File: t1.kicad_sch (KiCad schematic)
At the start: 47 parts, among them J1 Barrel_Jack_Switch, J2 USB_B, J3 P1, J4 2x2M, J5 ICSP1, J6 P2, U1 ATmega8U2-AU, Y1 16MHz

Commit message: Updated symbols to the ones currently used by KiCad
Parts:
- C1: symbol Device:CP -> Device:C_Polarized
- FB1: symbol Device:Ferrite_Bead -> Device:FerriteBead
- U1: symbol MCU_Microchip_ATmega:ATmega8U2-AU -> MCU_Microchip_ATmega:ATmega8U2-A
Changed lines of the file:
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@@
     (effects (font (size 1.27 1.27)) (justify left bottom))
   )
-  (symbol (lib_id "MCU_Microchip_ATmega:ATmega8U2-AU") (at 162.56 100.33 0) (unit 1)
+  (symbol (lib_id "MCU_Microchip_ATmega:ATmega8U2-A") (at 162.56 100.33 0) (unit 1)
     (in_bom yes) (on_board yes)
     (property "Reference" "U1" (id 0) (at 148.59 66.04 0))
@@
     (pin "2")
   )
-  (symbol (lib_id "Device:Ferrite_Bead") (at 96.52 130.81 0) (unit 1)
+  (symbol (lib_id "Device:FerriteBead") (at 96.52 130.81 0) (unit 1)
     (in_bom yes) (on_board yes)
     (property "Reference" "FB1" (id 0) (at 99.9998 129.6416 0)
@@
     (pin "1")
   )
-  (symbol (lib_id "Device:CP") (at 82.55 53.34 0) (unit 1)
+  (symbol (lib_id "Device:C_Polarized") (at 82.55 53.34 0) (unit 1)
     (in_bom yes) (on_board yes)
     (property "Reference" "C1" (id 0) (at 85.5472 52.1716 0)

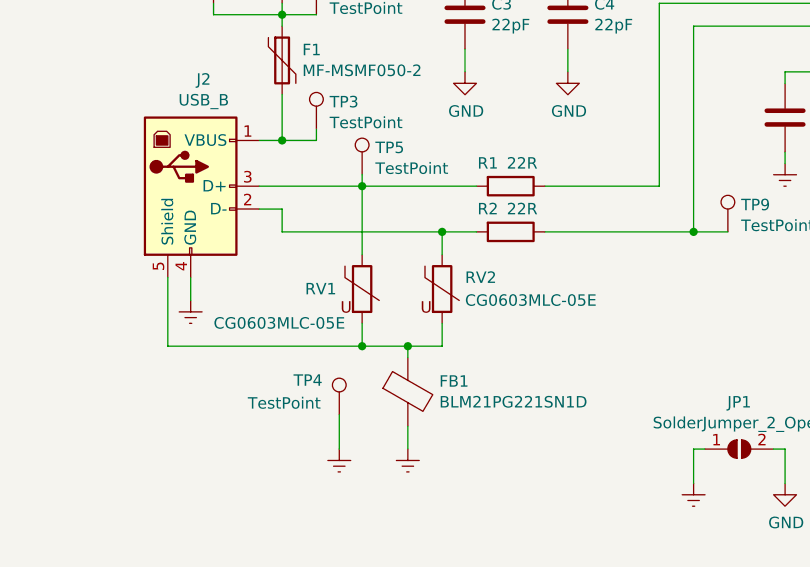
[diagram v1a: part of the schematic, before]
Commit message: Renamed varistors from RV to VR (not potentiometers)
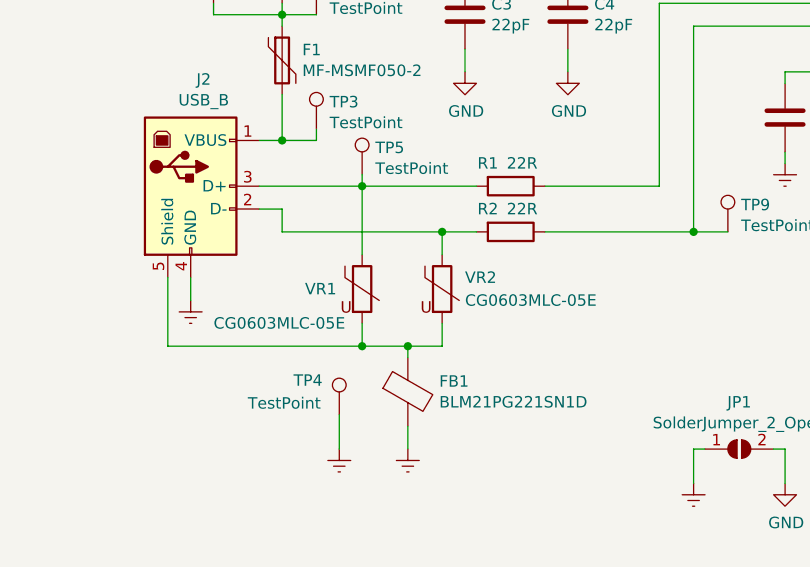
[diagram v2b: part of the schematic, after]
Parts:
- renumbered RV1 to VR1, RV2 to VR2
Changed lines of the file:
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@@
   (symbol (lib_id "Device:Varistor") (at 100.33 119.38 0) (unit 1)
     (in_bom yes) (on_board yes)
-    (property "Reference" "RV2" (id 0) (at 102.87 118.11 0)
+    (property "Reference" "VR2" (id 0) (at 102.87 118.11 0)
       (effects (font (size 1.27 1.27)) (justify left))
     )
@@
   (symbol (lib_id "Device:Varistor") (at 91.44 119.38 0) (unit 1)
     (in_bom yes) (on_board yes)
-    (property "Reference" "RV1" (id 0) (at 85.09 119.38 0)
+    (property "Reference" "VR1" (id 0) (at 85.09 119.38 0)
       (effects (font (size 1.27 1.27)) (justify left))
     )
@@
       (reference "R7") (unit 1) (value "1K") (footprint "Resistor_SMD:R_0805_2012Metric")
     )
-    (path "/00000000-0000-0000-0000-00005f5a461f"
-      (reference "RV1") (unit 1) (value "CG0603MLC-05E") (footprint "Resistor_SMD:R_0603_1608Metric")
-    )
-    (path "/00000000-0000-0000-0000-00005f596a91"
-      (reference "RV2") (unit 1) (value "CG0603MLC-05E") (footprint "Resistor_SMD:R_0603_1608Metric")
-    )
     (path "/00000000-0000-0000-0000-00005f5b39e3"
       (reference "TP2") (unit 1) (value "TestPoint") (footprint "TestPoint:TestPoint_Pad_D1.0mm")
@@
       (reference "U1") (unit 1) (value "ATmega8U2-AU") (footprint "Package_QFP:TQFP-32_7x7mm_P0.8mm")
     )
+    (path "/00000000-0000-0000-0000-00005f5a461f"
+      (reference "VR1") (unit 1) (value "CG0603MLC-05E") (footprint "Resistor_SMD:R_0603_1608Metric")
+    )
+    (path "/00000000-0000-0000-0000-00005f596a91"
+      (reference "VR2") (unit 1) (value "CG0603MLC-05E") (footprint "Resistor_SMD:R_0603_1608Metric")
+    )
     (path "/00000000-0000-0000-0000-00005f598bfc"
